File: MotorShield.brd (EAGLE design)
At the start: 85 x 56 mm, 89 parts, among them IC1 OPA4340E, IC2 OPA4340E, IC3 74HCT125D

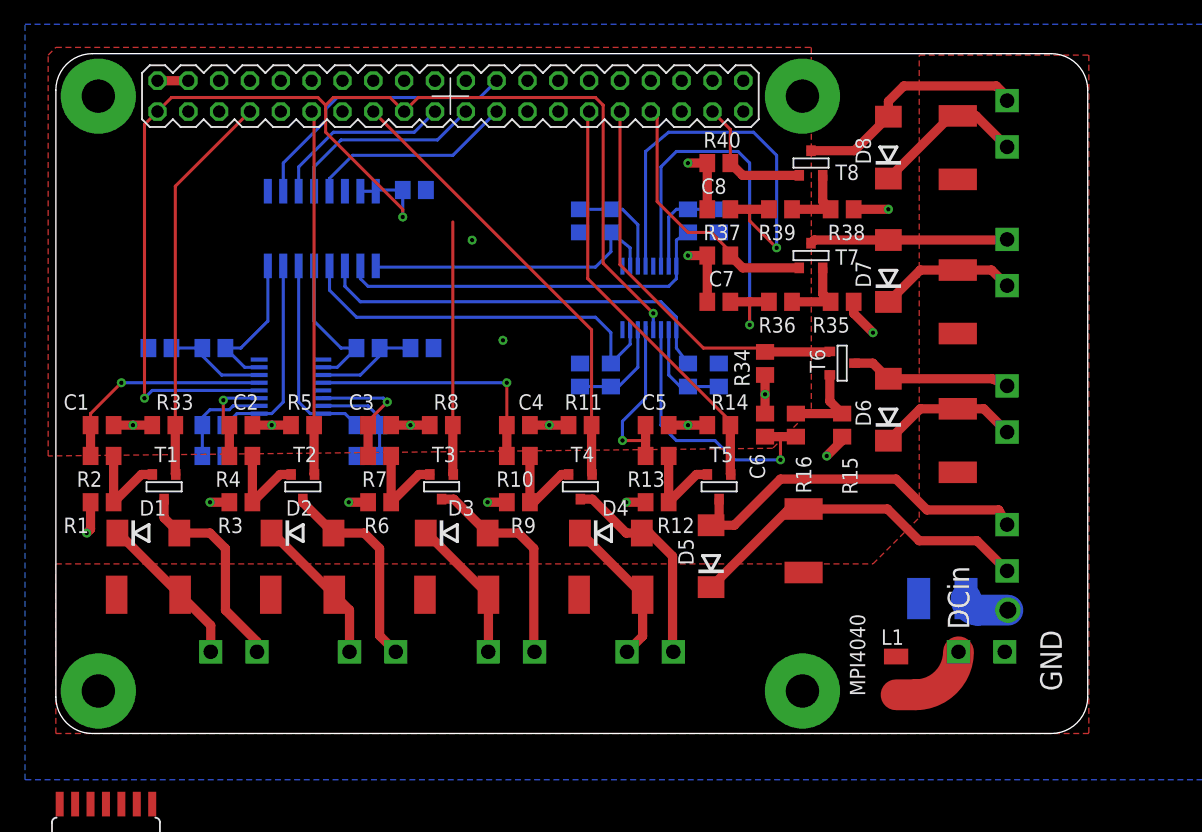
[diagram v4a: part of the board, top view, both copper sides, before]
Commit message: changed connectors fixes #12
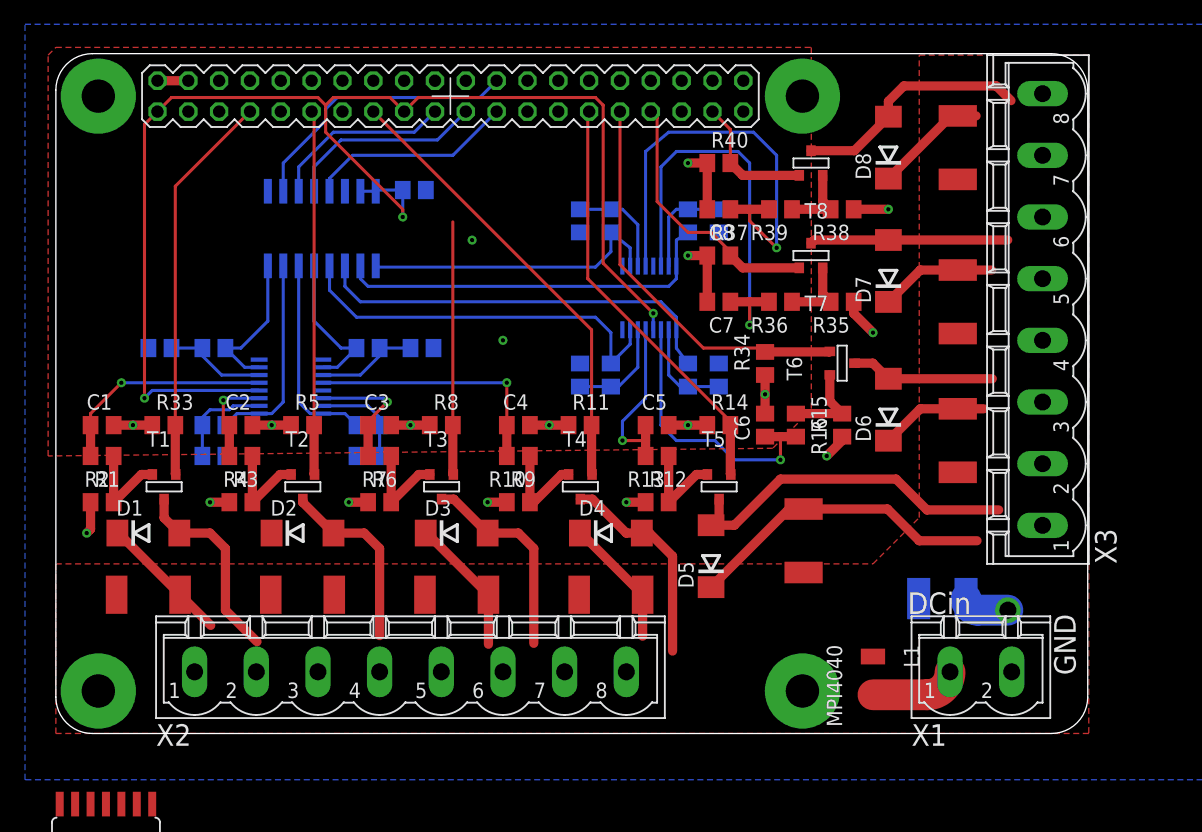
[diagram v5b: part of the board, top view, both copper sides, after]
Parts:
- removed U$1, U$16, U$2, U$3, U$34, U$4, U$5, U$6, U$7: AKL-BUCHSE, Anschluss:AKL-BUCHSE
- added X1: MSTBV2, con-phoenix-508:MSTBV2
- added X2, X3: MSTBV8, con-phoenix-508:MSTBV8
- moved L1 1.91 mm to (67.3, 4.76)
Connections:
- removed net N$28: L1.P$1, U$16.PLUS
- new net N$23: L1.P$1, X1.1
- net 24V/1A: now also X2.1; no longer U$34.PLUS
- net GND: now also X1.2; no longer U$16.MINUS
- net N$10: now also X2.4; no longer U$1.MINUS
- net N$12: now also X2.5; no longer U$2.PLUS
- net N$13: now also X2.3; no longer U$1.PLUS
- net N$17: now also X2.6; no longer U$2.MINUS
- net N$2: now also X2.2; no longer U$34.MINUS
- net N$26: now also X2.8; no longer U$3.MINUS
- net N$38: now also X3.2; no longer U$4.MINUS
- net N$4: now also X3.7; no longer U$7.PLUS
- net N$45: now also X3.4; no longer U$5.MINUS
- net N$5: now also X3.5; no longer U$6.PLUS
- net N$51: now also X3.6; no longer U$6.MINUS
- net N$57: now also X3.8; no longer U$7.MINUS
- net N$7: now also X3.3; no longer U$5.PLUS
- net N$8: now also X3.1; no longer U$4.PLUS
- net N$9: now also X2.7; no longer U$3.PLUS
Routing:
- net N$13: track 12.5 -> 0.09 mm
- net N$23: track 0.00 -> 7.13 mm
- net N$28: track 6.61 -> 0.00 mm
- net N$4: track 13.0 -> 9.36 mm
- net N$8: track 29.1 -> 25.6 mm
- net N$7: track 11.7 -> 8.95 mm
- net 24V/1A: track 13.0 -> 10.8 mm
- net N$10: track 17.2 -> 15.3 mm
- net N$9: track 12.5 -> 10.7 mm
- net N$5: track 11.4 -> 9.58 mm
- net N$38: track 30.1 -> 28.7 mm
- net N$45: track 13.2 -> 11.9 mm
- net N$2: track 17.2 -> 16.4 mm
- net N$17: track 17.8 -> 17.1 mm
- net N$12: track 12.0 -> 11.3 mm

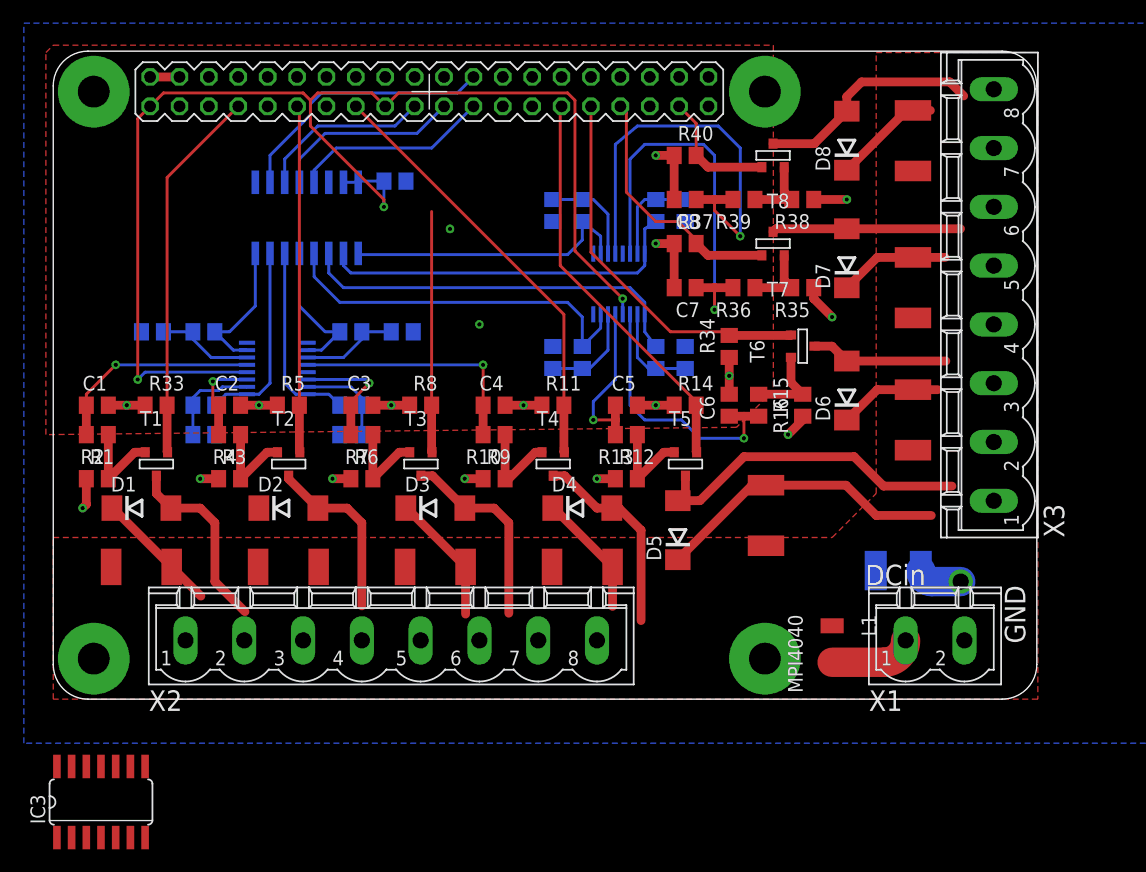
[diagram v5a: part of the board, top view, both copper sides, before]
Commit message: added connectors for inputs, button LED and dotstars fixes #7
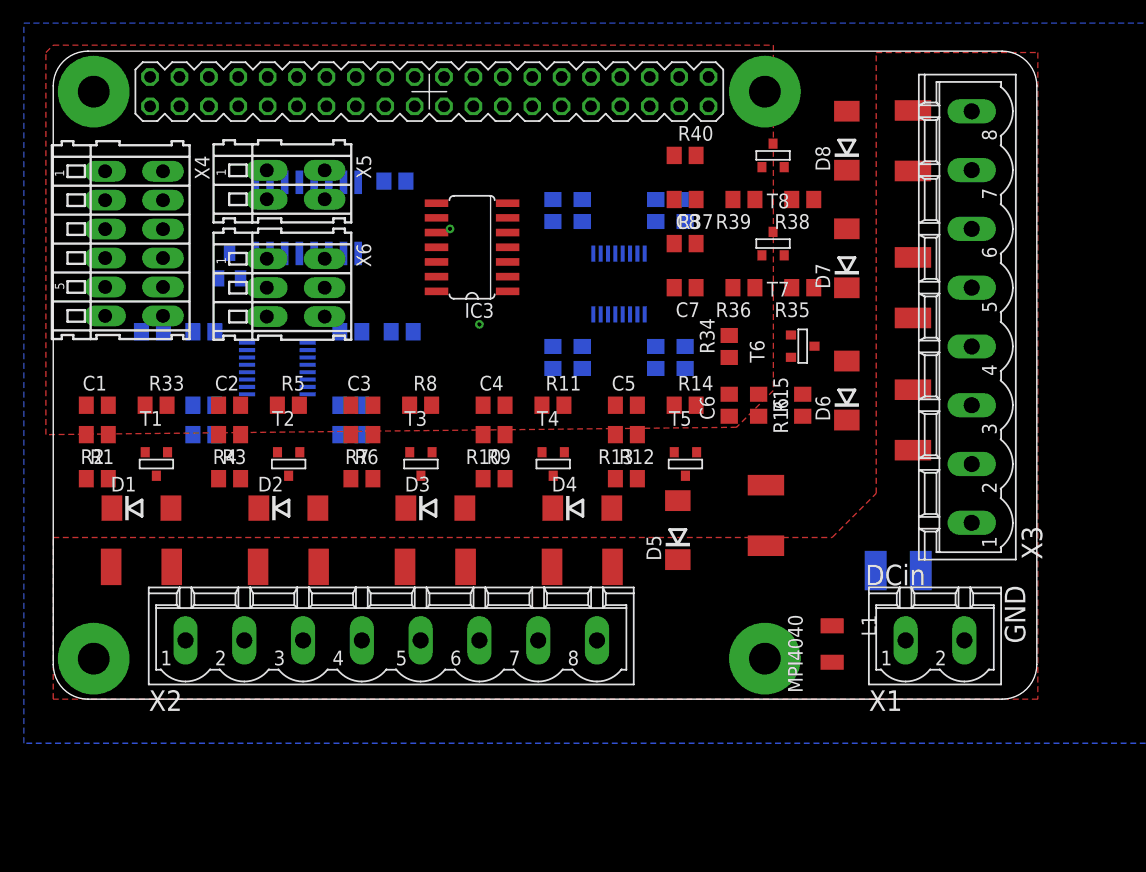
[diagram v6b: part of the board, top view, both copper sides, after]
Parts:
- added T9: (no value), transistor:SOT23-BEC
- added X4: INPUTS, con-wago255:233-206
- added X5: BUTTON_LED, con-wago255:233-202
- added X6: DOTSTARS, con-wago255:233-203
- moved IC3 57.7 mm to (36.2, 39.1), turned to 90 degrees
- moved X3 2.69 mm to (79.4, 33.0)
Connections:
- removed net 24V/8A: C10.1, F1.P$2, F2.P$2, F3.P$2, F4.P$2, F5.P$2, F6.P$2, F7.P$2, F8.P$2, L1.P$2
- new net +24V: C10.1, F1.P$2, F2.P$2, F3.P$2, F4.P$2, F5.P$2, F6.P$2, F7.P$2, F8.P$2, L1.P$2, X5.A1
- new net INP_BTN_START: X4.A1
- new net INP_DOOR_CTRL: X4.A3
- new net INP_DOOR_JUICE: X4.A5
- new net N$32: T9.C, X5.A2
- new net N$33: T9.B
- net DOTCLK: now also X6.A2
- net DOTDAT: now also X6.A3
- net GND: now also T9.E, X4.A2, X4.A4, X4.A6, X6.A1
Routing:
- net 3,3V: track 110.5 -> 0.00 mm, vias 3 -> 0
- net GND: track 47.1 -> 0.00 mm, vias 16 -> 0
- net M4: track 37.4 -> 0.00 mm
- net V0: track 36.5 -> 0.00 mm, vias 1 -> 0
- net M3: track 34.8 -> 0.00 mm
- net V1: track 34.8 -> 0.00 mm, vias 1 -> 0
- net CH2: track 34.2 -> 0.00 mm
- net M2: track 32.9 -> 0.00 mm
- net CH3: track 32.6 -> 0.00 mm
- net CH1: track 32.6 -> 0.00 mm
- net M7: track 32.5 -> 0.00 mm
- net M6: track 30.0 -> 0.00 mm
- net N$38: track 28.7 -> 0.00 mm
- net N$8: track 25.6 -> 0.00 mm
- net CH0: track 25.1 -> 0.00 mm
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
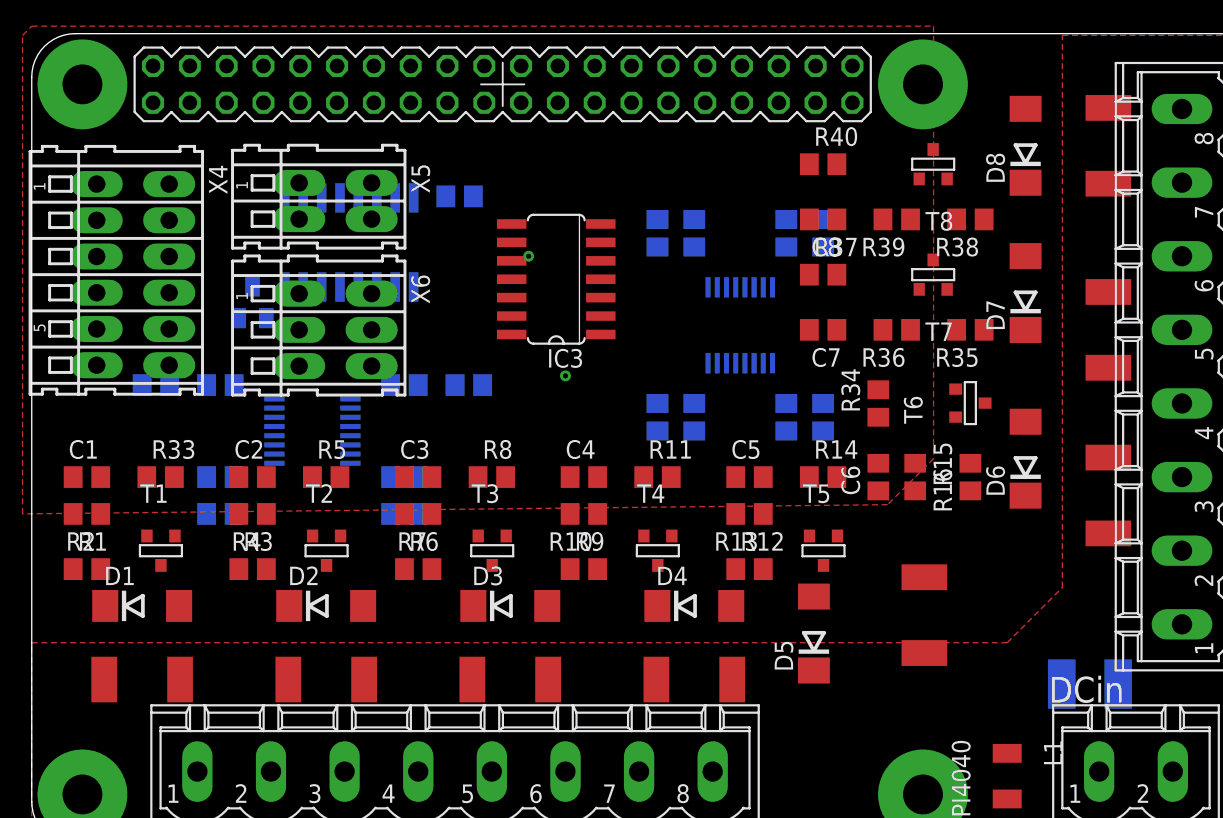
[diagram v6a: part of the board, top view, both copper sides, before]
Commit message: changed fuse library to ptc-litlefuse from https://github.com/halfakop/eagle-lbr
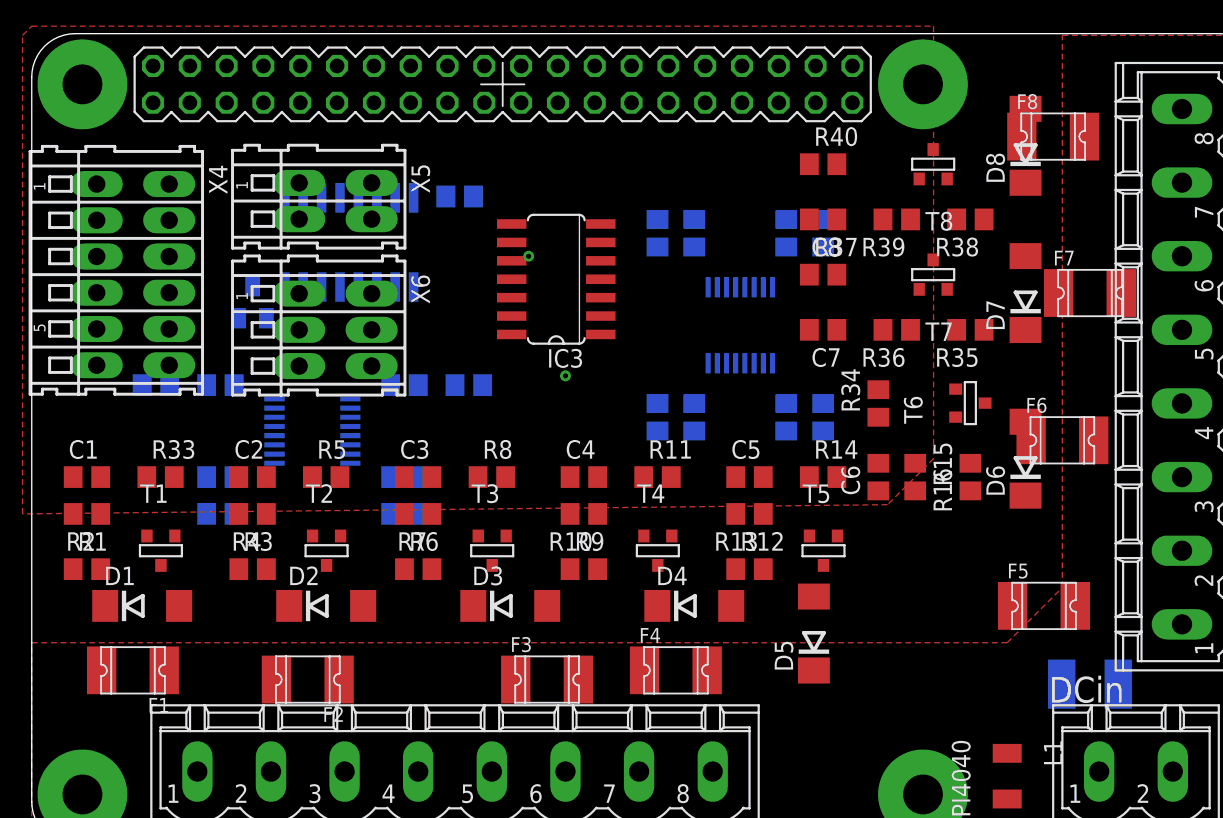
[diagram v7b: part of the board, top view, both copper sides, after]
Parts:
- F1, F2, F3, F4, F5, F6, F7, F8: value POLY-FUSE -> 1812L; device SMD-Fuse:1812L050 -> ptc-littlefuse:1812L
- moved F5 8.28 mm to (69.8, 16.5), turned to 0 degrees
- moved F6 4.96 mm to (71.1, 27.9), turned to 0 degrees
- moved F8 3.86 mm to (70.5, 48.9), turned to 0 degrees
- moved F7 2.84 mm to (73.0, 38.1), turned to 0 degrees
- moved F3 2.54 mm to (35.6, 11.4), turned to 0 degrees
- moved F4 1.42 mm to (44.5, 12.1), turned to 0 degrees
- moved F2 1.27 mm to (19.1, 11.4)
- moved F1 0.90 mm to (6.99, 12.1)
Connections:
- net +24V: now also F1.2, F2.2, F3.2, F4.2, F5.2, F6.2, F7.2, F8.2; no longer F1.P$2, F2.P$2, F3.P$2, F4.P$2, F5.P$2, F6.P$2, F7.P$2, F8.P$2
- net 24V/1A: now also F1.1; no longer F1.P$1
- net N$12: now also F3.1; no longer F3.P$1
- net N$13: now also F2.1; no longer F2.P$1
- net N$4: now also F8.1; no longer F8.P$1
- net N$5: now also F7.1; no longer F7.P$1
- net N$7: now also F6.1; no longer F6.P$1
- net N$8: now also F5.1; no longer F5.P$1
- net N$9: now also F4.1; no longer F4.P$1
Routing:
- added copper zone on layer 1, net +24V
- removed copper zone on layer 1, net 24V/8A
